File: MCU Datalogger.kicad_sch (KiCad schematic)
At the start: 25 parts, among them U1 24LC1025, U2 DS1337S_, U3 24LC1025, U4 ATMEGA328P-AU, Y1 32.768 MHz, Y2 16 MHz

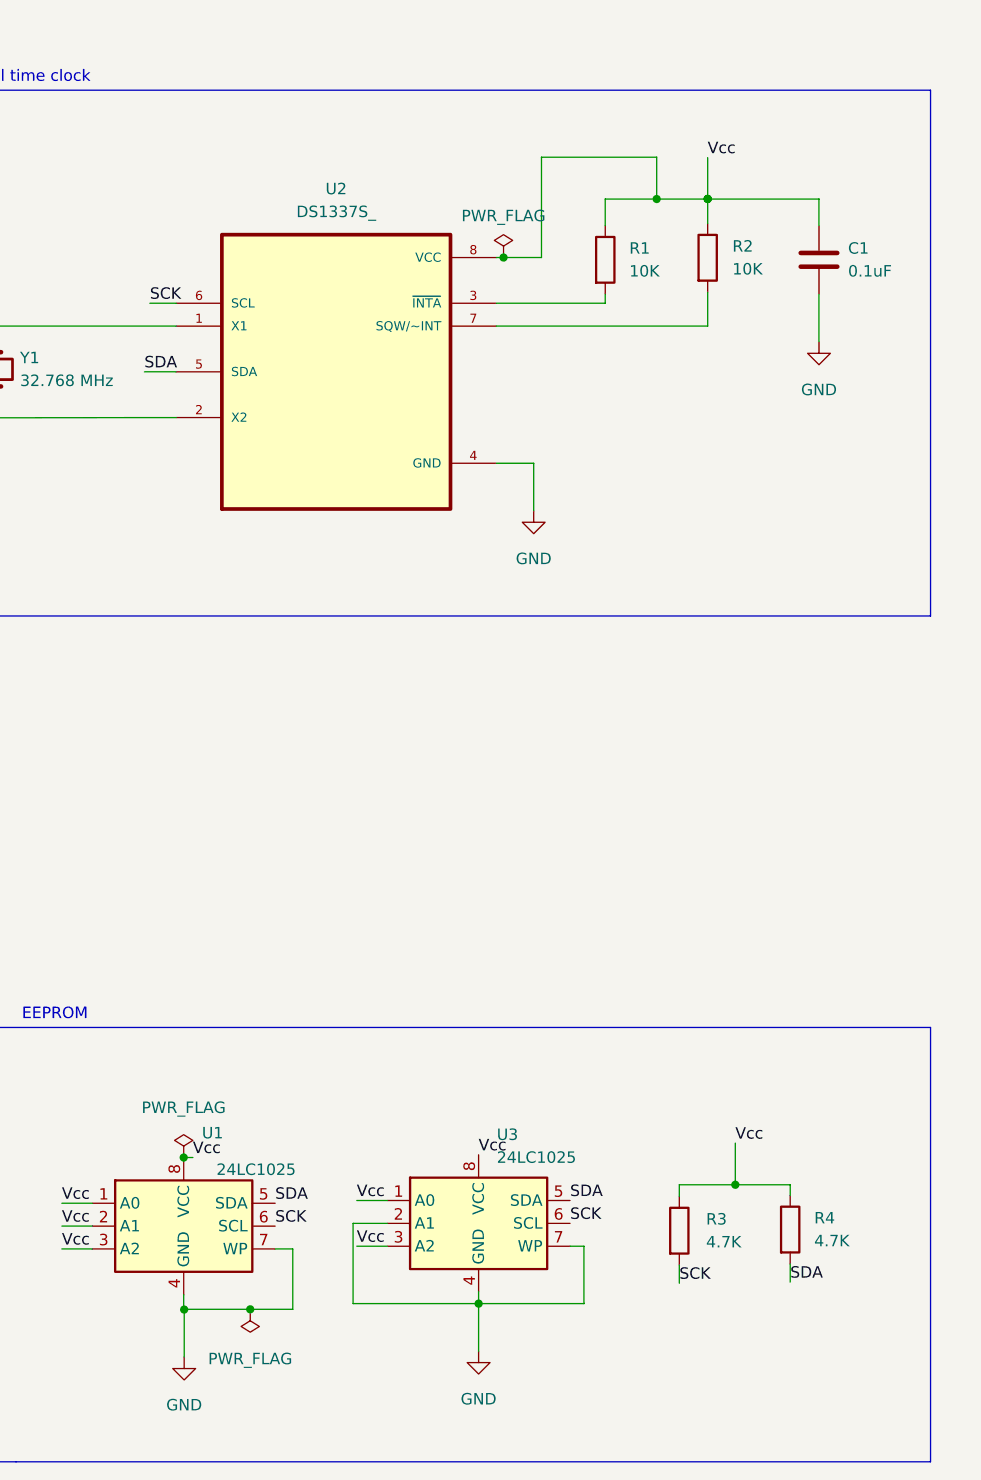
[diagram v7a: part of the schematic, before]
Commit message: Routing sans GND Vcc complete.
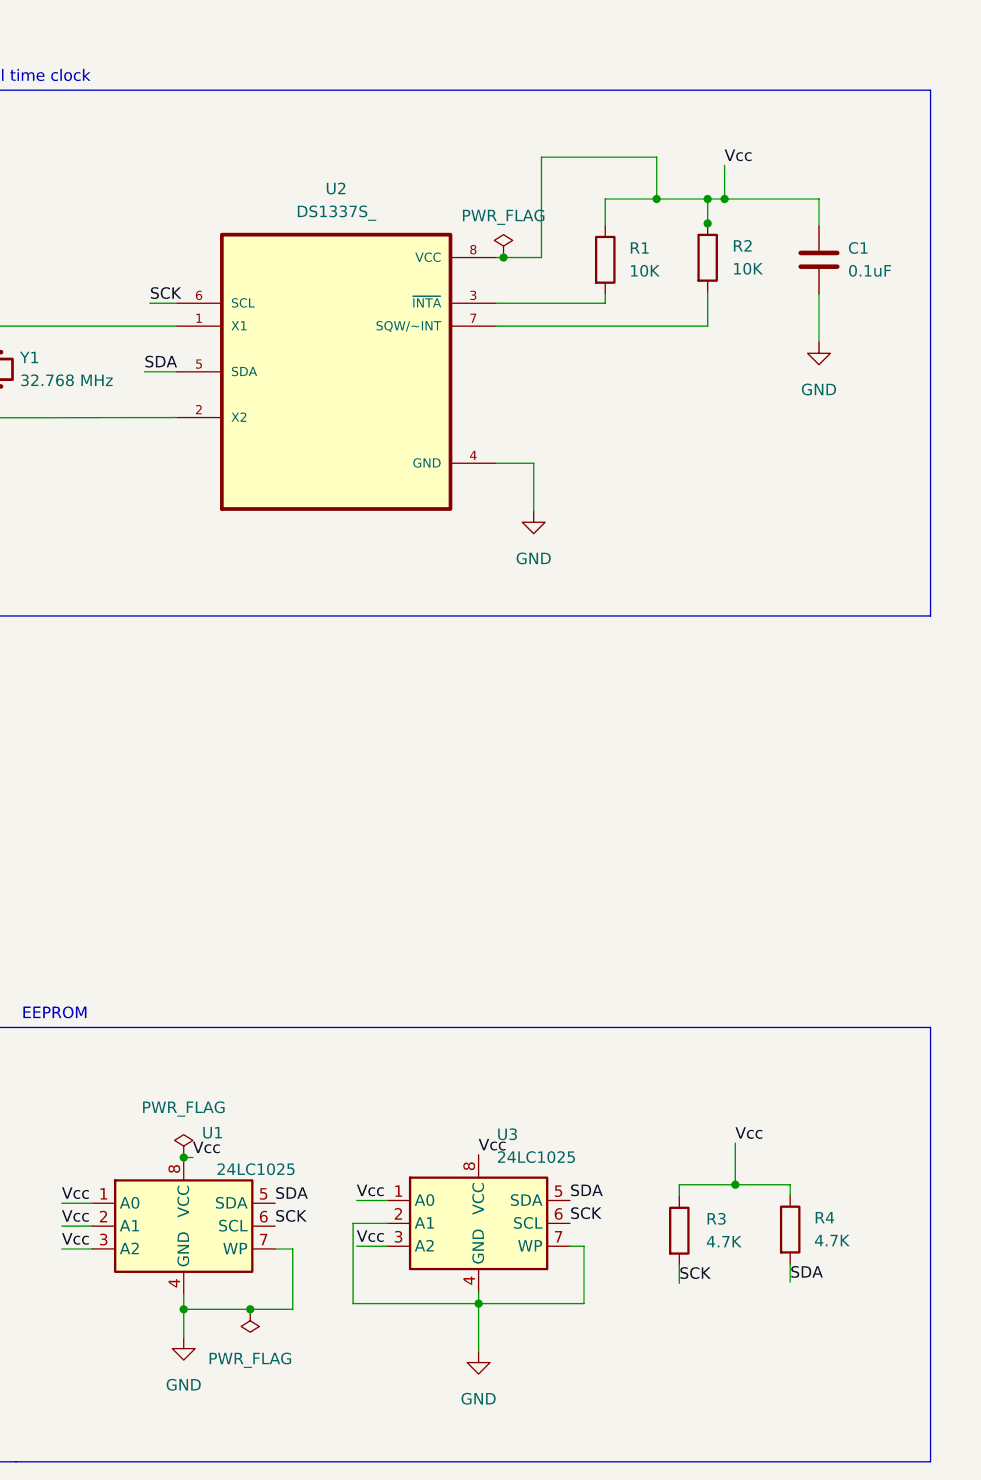
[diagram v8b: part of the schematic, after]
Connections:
- net GND: now also U1.4 (GND), U1.7 (WP)
- net Vcc: now also C1.1, R1.1, R2.1, U2.8 (VCC)
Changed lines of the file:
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@@
   (junction (at 240.3856 33.02) (diameter 0) (color 0 0 0 0)
   )
+  (junction (at 101.5746 34.9504) (diameter 0) (color 0 0 0 0)
+  )
   (junction (at 156.8704 84.5566) (diameter 0) (color 0 0 0 0)
   )
-  (junction (at 99.695 34.925) (diameter 0) (color 0 0 0 0)
-  )
   (junction (at 228.5238 33.02) (diameter 0) (color 0 0 0 0)
   )
   (junction (at 263.2964 44.704) (diameter 0) (color 0 0 0 0)
   )
-  (junction (at 41.529 158.3436) (diameter 0) (color 0 0 0 0)
+  (junction (at 41.4782 158.3182) (diameter 0) (color 0 0 0 0)
   )
   (junction (at 94.0308 34.9504) (diameter 0) (color 0 0 0 0)
@@
   (junction (at 251.0028 33.02) (diameter 0) (color 0 0 0 0)
   )
+  (junction (at 99.695 34.9504) (diameter 0) (color 0 0 0 0)
+  )
   (junction (at 41.4782 141.4526) (diameter 0) (color 0 0 0 0)
   )
@@
   (junction (at 74.2442 157.6832) (diameter 0) (color 0 0 0 0)
   )
-  (junction (at 99.695 34.9504) (diameter 0) (color 0 0 0 0)
+  (junction (at 99.695 37.6682) (diameter 0) (color 0 0 0 0)
   )
   (junction (at 142.24 55.88) (diameter 0) (color 0 0 0 0)
@@
     (stroke (width 0) (type default) (color 0 0 0 0))
   )
+  (wire (pts (xy 99.695 37.6936) (xy 99.695 37.6682))
+    (stroke (width 0) (type default) (color 0 0 0 0))
+  )
   (wire (pts (xy 239.3188 69.5452) (xy 239.3188 74.8538))
     (stroke (width 0) (type default) (color 0 0 0 0))
@@
     (stroke (width 0) (type default) (color 0 0 0 0))
   )
-  (wire (pts (xy 99.695 30.353) (xy 99.695 34.925))
+  (wire (pts (xy 101.5746 31.2166) (xy 101.5746 34.9504))
     (stroke (width 0) (type default) (color 0 0 0 0))
   )
@@
     (stroke (width 0) (type default) (color 0 0 0 0))
   )
-  (wire (pts (xy 112.0648 34.9504) (xy 99.695 34.9504))
+  (wire (pts (xy 94.0308 34.9504) (xy 99.695 34.9504))
     (stroke (width 0) (type default) (color 0 0 0 0))
   )
@@
     (stroke (width 0) (type default) (color 0 0 0 0))
   )
+  (wire (pts (xy 41.4782 158.3182) (xy 41.4782 161.417))
+    (stroke (width 0) (type default) (color 0 0 0 0))
+  )
   (wire (pts (xy 168.1226 70.2818) (xy 173.7614 70.2818))
     (stroke (width 0) (type default) (color 0 0 0 0))
@@
     (stroke (width 0) (type default) (color 0 0 0 0))
   )
-  (wire (pts (xy 99.695 37.6682) (xy 99.695 34.9504))
+  (wire (pts (xy 99.695 34.9504) (xy 99.695 37.6682))
     (stroke (width 0) (type default) (color 0 0 0 0))
   )
@@
     (stroke (width 0) (type default) (color 0 0 0 0))
   )
-  (wire (pts (xy 41.529 158.3436) (xy 41.529 163.6268))
-    (stroke (width 0) (type default) (color 0 0 0 0))
-  )
   (wire (pts (xy 185.42 37.465) (xy 185.42 35.56))
     (stroke (width 0) (type default) (color 0 0 0 0))
@@
     (stroke (width 0) (type default) (color 0 0 0 0))
   )
+  (wire (pts (xy 99.695 34.9504) (xy 101.5746 34.9504))
+    (stroke (width 0) (type default) (color 0 0 0 0))
+  )
   (wire (pts (xy 180.34 55.88) (xy 177.8 55.88))
     (stroke (width 0) (type default) (color 0 0 0 0))
@@
     (stroke (width 0) (type default) (color 0 0 0 0))
   )
-  (wire (pts (xy 41.4782 158.3182) (xy 41.4782 156.6926))
+  (wire (pts (xy 41.4782 156.6926) (xy 41.4782 158.3182))
     (stroke (width 0) (type default) (color 0 0 0 0))
   )
@@
     (stroke (width 0) (type default) (color 0 0 0 0))
   )
-  (wire (pts (xy 99.695 34.9504) (xy 94.0308 34.9504))
-    (stroke (width 0) (type default) (color 0 0 0 0))
-  )
   (wire (pts (xy 27.94 151.6126) (xy 31.3182 151.6126))
     (stroke (width 0) (type default) (color 0 0 0 0))
@@
   )
   (wire (pts (xy 187.5282 84.5566) (xy 187.5282 58.42))
+    (stroke (width 0) (type default) (color 0 0 0 0))
+  )
+  (wire (pts (xy 101.5746 34.9504) (xy 112.0648 34.9504))
     (stroke (width 0) (type default) (color 0 0 0 0))
   )
@@
     (effects (font (size 1.27 1.27)) (justify left bottom))
   )
-  (label "Vcc" (at 99.695 30.353 0)
+  (label "Vcc" (at 101.5746 31.2166 0)
     (effects (font (size 1.27 1.27)) (justify left bottom))
   )
@@
     (pin "2")
   )
-  (symbol (lib_id "power:GND") (at 41.529 163.6268 0) (unit 1)
-    (in_bom yes) (on_board yes) (fields_autoplaced)
-    (property "Reference" "#PWR01" (id 0) (at 41.529 169.9768 0)
-      (effects (font (size 1.27 1.27)) hide)
-    )
-    (property "Value" "GND" (id 1) (at 41.529 168.9608 0))
-    (property "Footprint" "" (id 2) (at 41.529 163.6268 0)
-      (effects (font (size 1.27 1.27)) hide)
-    )
-    (property "Datasheet" "" (id 3) (at 41.529 163.6268 0)
-      (effects (font (size 1.27 1.27)) hide)
-    )
+  (symbol (lib_id "power:GND") (at 41.4782 161.417 0) (unit 1)
+    (in_bom yes) (on_board yes) (fields_autoplaced)
+    (property "Reference" "#PWR01" (id 0) (at 41.4782 167.767 0)
+      (effects (font (size 1.27 1.27)) hide)
+    )
+    (property "Value" "GND" (id 1) (at 41.4782 166.751 0))
+    (property "Footprint" "" (id 2) (at 41.4782 161.417 0)
+      (effects (font (size 1.27 1.27)) hide)
+    )
+    (property "Datasheet" "" (id 3) (at 41.4782 161.417 0)
+      (effects (font (size 1.27 1.27)) hide)
+    )
